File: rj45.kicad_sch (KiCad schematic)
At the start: 6 parts, among them J6 RJ45_HC612601A-M893-A

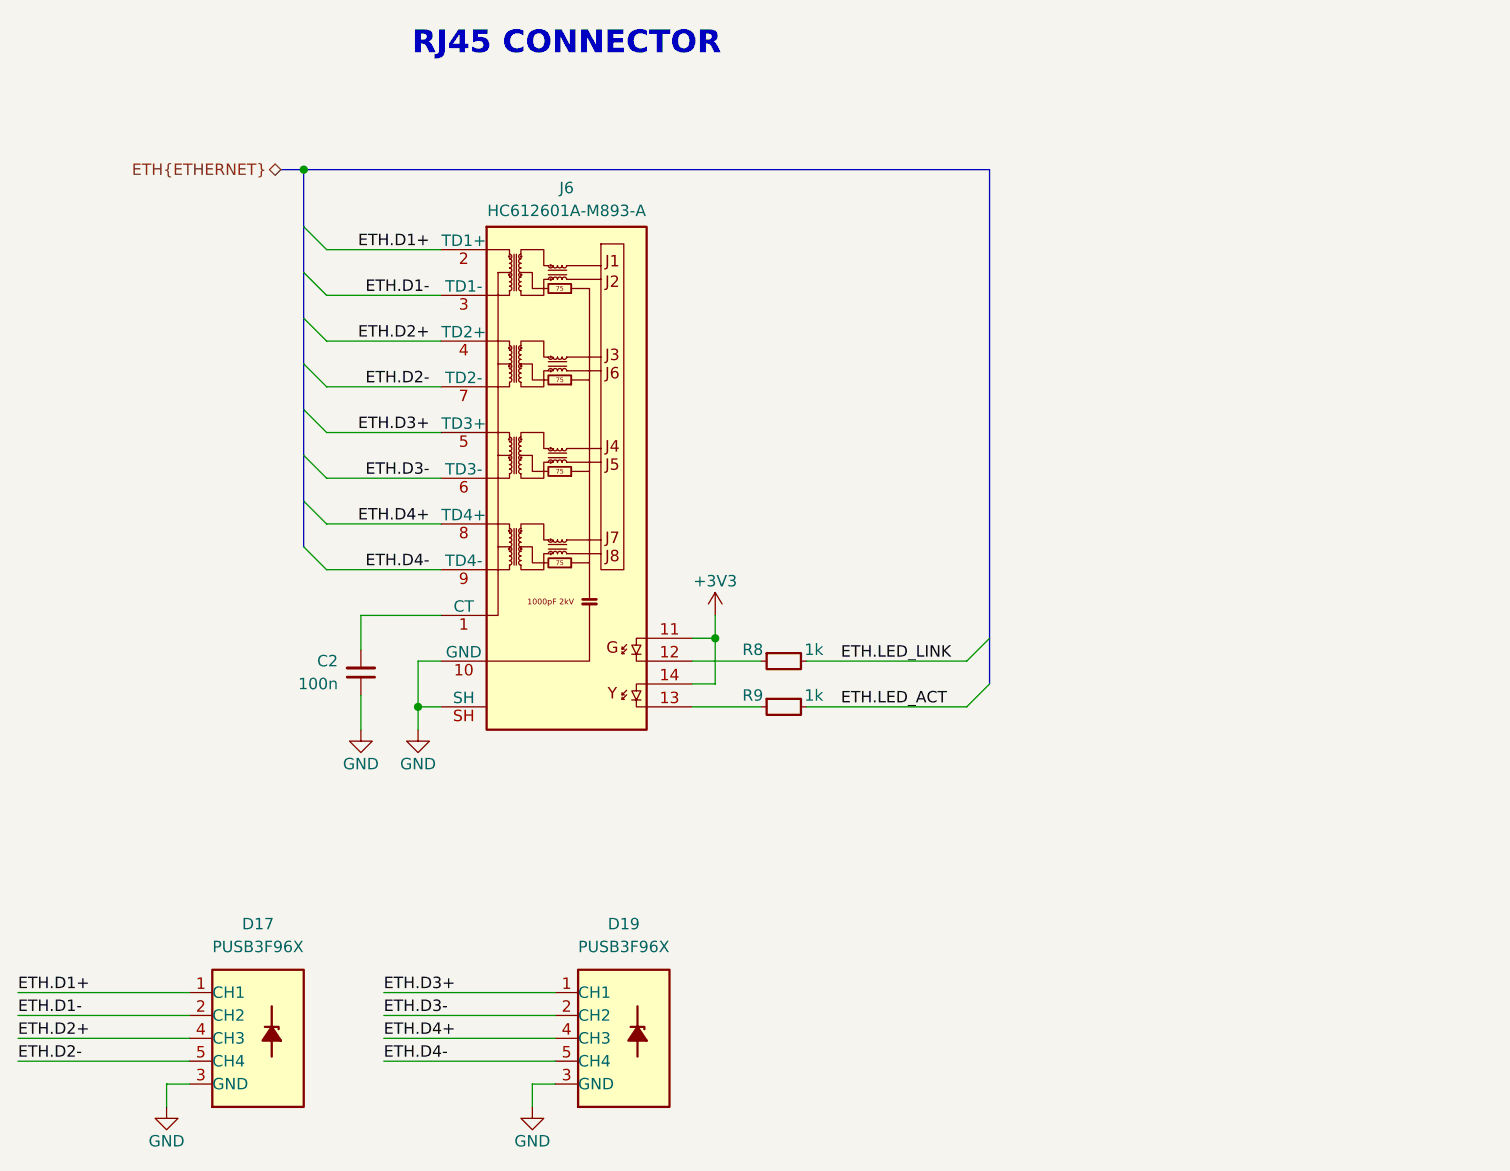
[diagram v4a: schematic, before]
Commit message: [#3] WIP: Clear ERC, re-annotate schematic
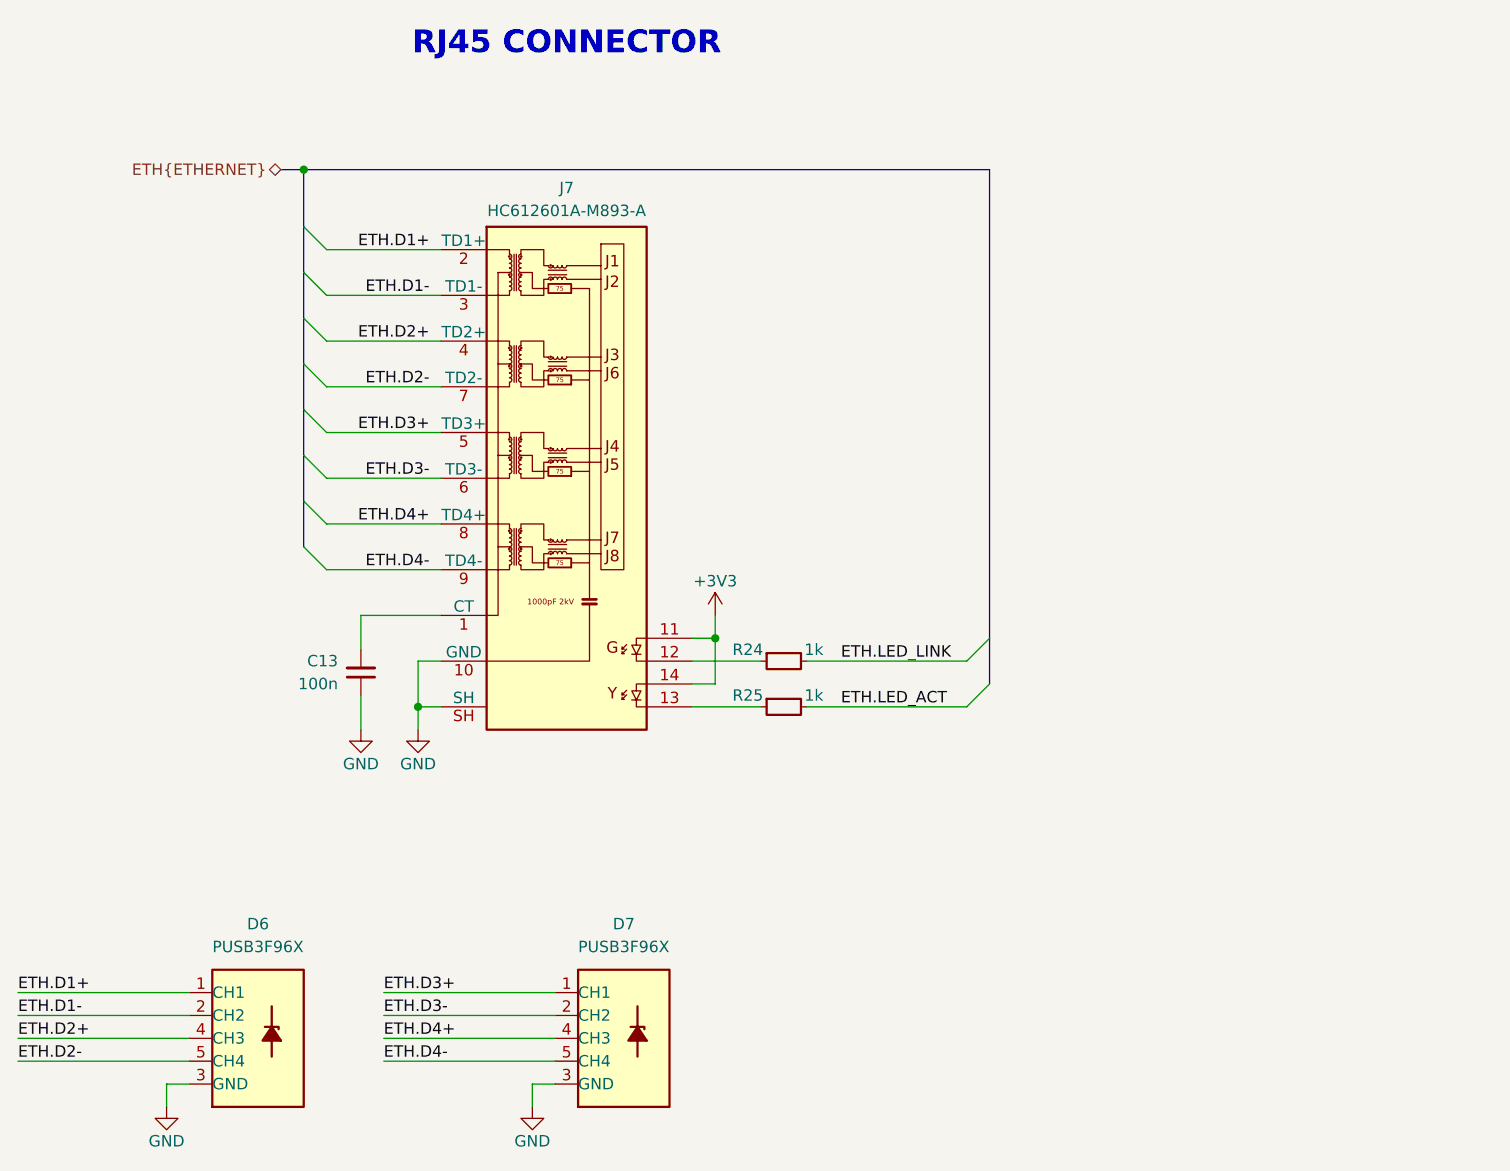
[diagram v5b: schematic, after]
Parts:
- renumbered C2 to C13, D17 to D6, D19 to D7, J6 to J7, R8 to R24, R9 to R25
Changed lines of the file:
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@@
 		(on_board yes)
 		(dnp no)
-		(property "Reference" "#PWR0193"
+		(property "Reference" "#PWR057"
 			(at 102.87 184.15 0)
 			(effects
@@
 			(project "cm5-module"
 				(path "/090a8e41-87a8-4fb1-998b-60a2c0dc4cee/dd50f821-f925-406c-ae05-a2a500dfc6d6"
-					(reference "#PWR0193")
+					(reference "#PWR057")
 					(unit 1)
 				)
@@
 		(on_board yes)
 		(dnp no)
-		(property "Reference" "#PWR031"
+		(property "Reference" "#PWR056"
 			(at 130.81 142.24 0)
 			(effects
@@
 			(project "cm5-module"
 				(path "/090a8e41-87a8-4fb1-998b-60a2c0dc4cee/dd50f821-f925-406c-ae05-a2a500dfc6d6"
-					(reference "#PWR031")
+					(reference "#PWR056")
 					(unit 1)
 				)
@@
 		(on_board yes)
 		(dnp no)
-		(property "Reference" "#PWR029"
+		(property "Reference" "#PWR054"
 			(at 163.83 127 0)
 			(effects
@@
 			(project ""
 				(path "/090a8e41-87a8-4fb1-998b-60a2c0dc4cee/dd50f821-f925-406c-ae05-a2a500dfc6d6"
-					(reference "#PWR029")
+					(reference "#PWR054")
 					(unit 1)
 				)
@@
 		(dnp no)
 		(fields_autoplaced yes)
-		(property "Reference" "D17"
+		(property "Reference" "D6"
 			(at 113.03 157.48 0)
 			(effects
@@
 			(project "cm5-module"
 				(path "/090a8e41-87a8-4fb1-998b-60a2c0dc4cee/dd50f821-f925-406c-ae05-a2a500dfc6d6"
-					(reference "D17")
+					(reference "D6")
 					(unit 1)
 				)
@@
 		(on_board yes)
 		(dnp no)
-		(property "Reference" "R9"
+		(property "Reference" "R25"
 			(at 169.164 132.08 0)
 			(effects
@@
 			(project "cm5-module"
 				(path "/090a8e41-87a8-4fb1-998b-60a2c0dc4cee/dd50f821-f925-406c-ae05-a2a500dfc6d6"
-					(reference "R9")
+					(reference "R25")
 					(unit 1)
 				)
@@
 		(on_board yes)
 		(dnp no)
-		(property "Reference" "R8"
+		(property "Reference" "R24"
 			(at 169.164 127 0)
 			(effects
@@
 			(project ""
 				(path "/090a8e41-87a8-4fb1-998b-60a2c0dc4cee/dd50f821-f925-406c-ae05-a2a500dfc6d6"
-					(reference "R8")
+					(reference "R24")
 					(unit 1)
 				)
@@
 		(on_board yes)
 		(dnp no)
-		(property "Reference" "#PWR0194"
+		(property "Reference" "#PWR058"
 			(at 143.51 184.15 0)
 			(effects
@@
 			(project "cm5-module"
 				(path "/090a8e41-87a8-4fb1-998b-60a2c0dc4cee/dd50f821-f925-406c-ae05-a2a500dfc6d6"
-					(reference "#PWR0194")
+					(reference "#PWR058")
 					(unit 1)
 				)
@@
 		(on_board yes)
 		(dnp no)
-		(property "Reference" "J6"
+		(property "Reference" "J7"
 			(at 147.32 75.692 0)
 			(effects
@@
 			(project ""
 				(path "/090a8e41-87a8-4fb1-998b-60a2c0dc4cee/dd50f821-f925-406c-ae05-a2a500dfc6d6"
-					(reference "J6")
+					(reference "J7")
 					(unit 1)
 				)
@@
 		(on_board yes)
 		(dnp no)
-		(property "Reference" "#PWR030"
+		(property "Reference" "#PWR055"
 			(at 124.46 142.24 0)
 			(effects
@@
 			(project "cm5-module"
 				(path "/090a8e41-87a8-4fb1-998b-60a2c0dc4cee/dd50f821-f925-406c-ae05-a2a500dfc6d6"
-					(reference "#PWR030")
+					(reference "#PWR055")
 					(unit 1)
 				)
@@
 		(on_board yes)
 		(dnp no)
-		(property "Reference" "C2"
+		(property "Reference" "C13"
 			(at 121.92 128.2636 90)
 			(effects
@@
 			(project "cm5-module"
 				(path "/090a8e41-87a8-4fb1-998b-60a2c0dc4cee/dd50f821-f925-406c-ae05-a2a500dfc6d6"
-					(reference "C2")
+					(reference "C13")
 					(unit 1)
 				)
@@
 		(dnp no)
 		(fields_autoplaced yes)
-		(property "Reference" "D19"
+		(property "Reference" "D7"
 			(at 153.67 157.48 0)
 			(effects
@@
 			(project "cm5-module"
 				(path "/090a8e41-87a8-4fb1-998b-60a2c0dc4cee/dd50f821-f925-406c-ae05-a2a500dfc6d6"
-					(reference "D19")
+					(reference "D7")
 					(unit 1)
 				)

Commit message: [#3] Re-annotate schematic
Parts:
- renumbered C13 to C76, D6 to D22, D7 to D23, J7 to J13, R24 to R83, R25 to R84
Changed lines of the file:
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@@
 		(on_board yes)
 		(dnp no)
-		(property "Reference" "#PWR057"
+		(property "Reference" "#PWR0194"
 			(at 102.87 184.15 0)
 			(effects
@@
 			(project "cm5-module"
 				(path "/090a8e41-87a8-4fb1-998b-60a2c0dc4cee/dd50f821-f925-406c-ae05-a2a500dfc6d6"
-					(reference "#PWR057")
+					(reference "#PWR0194")
 					(unit 1)
 				)
@@
 		(on_board yes)
 		(dnp no)
-		(property "Reference" "#PWR056"
+		(property "Reference" "#PWR0193"
 			(at 130.81 142.24 0)
 			(effects
@@
 			(project "cm5-module"
 				(path "/090a8e41-87a8-4fb1-998b-60a2c0dc4cee/dd50f821-f925-406c-ae05-a2a500dfc6d6"
-					(reference "#PWR056")
+					(reference "#PWR0193")
 					(unit 1)
 				)
@@
 		(on_board yes)
 		(dnp no)
-		(property "Reference" "#PWR054"
+		(property "Reference" "#PWR0191"
 			(at 163.83 127 0)
 			(effects
@@
 			(project ""
 				(path "/090a8e41-87a8-4fb1-998b-60a2c0dc4cee/dd50f821-f925-406c-ae05-a2a500dfc6d6"
-					(reference "#PWR054")
+					(reference "#PWR0191")
 					(unit 1)
 				)
@@
 		(dnp no)
 		(fields_autoplaced yes)
-		(property "Reference" "D6"
+		(property "Reference" "D22"
 			(at 113.03 157.48 0)
 			(effects
@@
 			(project "cm5-module"
 				(path "/090a8e41-87a8-4fb1-998b-60a2c0dc4cee/dd50f821-f925-406c-ae05-a2a500dfc6d6"
-					(reference "D6")
+					(reference "D22")
 					(unit 1)
 				)
@@
 		(on_board yes)
 		(dnp no)
-		(property "Reference" "R25"
+		(property "Reference" "R84"
 			(at 169.164 132.08 0)
 			(effects
@@
 			(project "cm5-module"
 				(path "/090a8e41-87a8-4fb1-998b-60a2c0dc4cee/dd50f821-f925-406c-ae05-a2a500dfc6d6"
-					(reference "R25")
+					(reference "R84")
 					(unit 1)
 				)
@@
 		(on_board yes)
 		(dnp no)
-		(property "Reference" "R24"
+		(property "Reference" "R83"
 			(at 169.164 127 0)
 			(effects
@@
 			(project ""
 				(path "/090a8e41-87a8-4fb1-998b-60a2c0dc4cee/dd50f821-f925-406c-ae05-a2a500dfc6d6"
-					(reference "R24")
+					(reference "R83")
 					(unit 1)
 				)
@@
 		(on_board yes)
 		(dnp no)
-		(property "Reference" "#PWR058"
+		(property "Reference" "#PWR0195"
 			(at 143.51 184.15 0)
 			(effects
@@
 			(project "cm5-module"
 				(path "/090a8e41-87a8-4fb1-998b-60a2c0dc4cee/dd50f821-f925-406c-ae05-a2a500dfc6d6"
-					(reference "#PWR058")
+					(reference "#PWR0195")
 					(unit 1)
 				)
@@
 		(on_board yes)
 		(dnp no)
-		(property "Reference" "J7"
+		(property "Reference" "J13"
 			(at 147.32 75.692 0)
 			(effects
@@
 			(project ""
 				(path "/090a8e41-87a8-4fb1-998b-60a2c0dc4cee/dd50f821-f925-406c-ae05-a2a500dfc6d6"
-					(reference "J7")
+					(reference "J13")
 					(unit 1)
 				)
@@
 		(on_board yes)
 		(dnp no)
-		(property "Reference" "#PWR055"
+		(property "Reference" "#PWR0192"
 			(at 124.46 142.24 0)
 			(effects
@@
 			(project "cm5-module"
 				(path "/090a8e41-87a8-4fb1-998b-60a2c0dc4cee/dd50f821-f925-406c-ae05-a2a500dfc6d6"
-					(reference "#PWR055")
+					(reference "#PWR0192")
 					(unit 1)
 				)
@@
 		(on_board yes)
 		(dnp no)
-		(property "Reference" "C13"
+		(property "Reference" "C76"
 			(at 121.92 128.2636 90)
 			(effects
@@
 			(project "cm5-module"
 				(path "/090a8e41-87a8-4fb1-998b-60a2c0dc4cee/dd50f821-f925-406c-ae05-a2a500dfc6d6"
-					(reference "C13")
+					(reference "C76")
 					(unit 1)
 				)
@@
 		(dnp no)
 		(fields_autoplaced yes)
-		(property "Reference" "D7"
+		(property "Reference" "D23"
 			(at 153.67 157.48 0)
 			(effects
@@
 			(project "cm5-module"
 				(path "/090a8e41-87a8-4fb1-998b-60a2c0dc4cee/dd50f821-f925-406c-ae05-a2a500dfc6d6"
-					(reference "D7")
+					(reference "D23")
 					(unit 1)
 				)

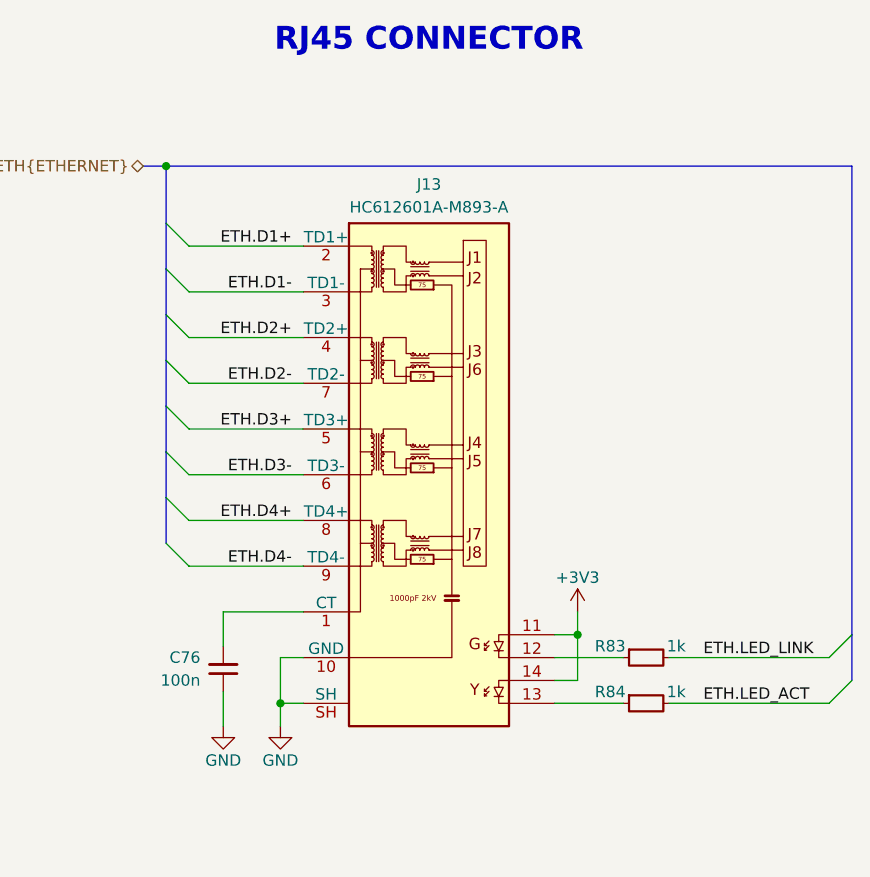
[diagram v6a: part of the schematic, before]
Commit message: [#3] Add GND pours on top and bottom
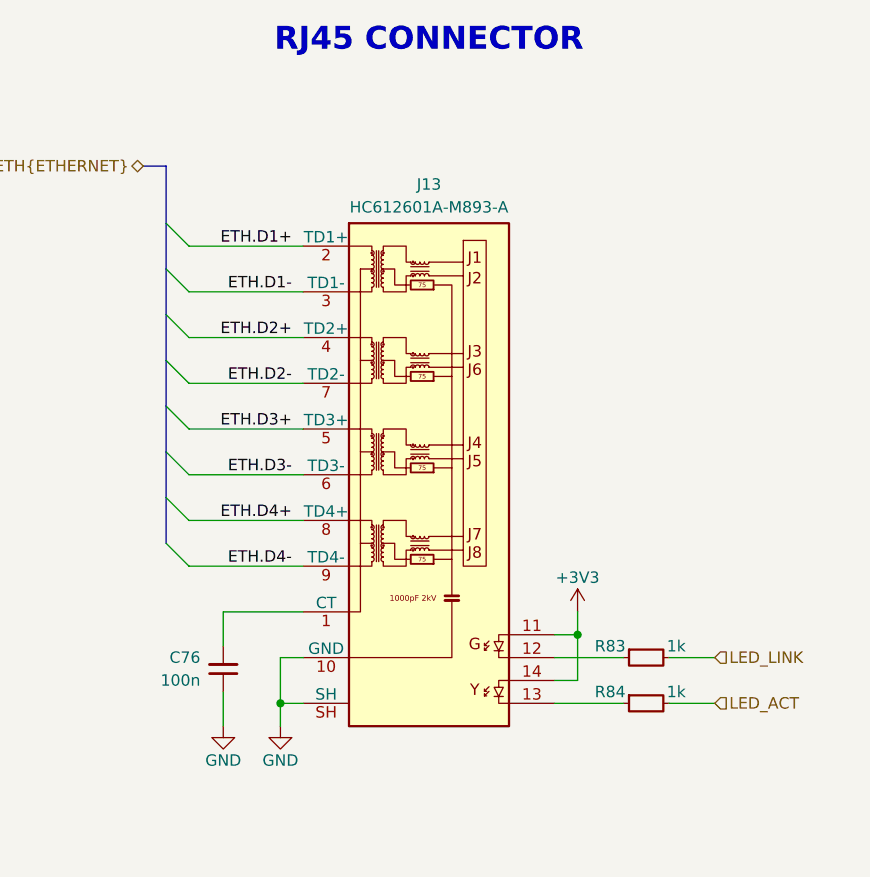
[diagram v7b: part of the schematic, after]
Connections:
- net ETH.LED_ACT renamed LED_ACT
- net ETH.LED_LINK renamed LED_LINK
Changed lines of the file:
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@@
-	)
-	(junction
-		(at 118.11 73.66)
-		(diameter 0)
-		(color 0 0 0 0)
 	)
 	(junction
@@
 	)
 	(bus_entry
-		(at 194.31 130.81)
-		(size -2.54 2.54)
-		(stroke
-			(width 0)
-			(type default)
-		)
-	)
-	(bus_entry
 		(at 120.65 107.95)
 		(size -2.54 -2.54)
@@
 		)
 	)
-	(bus_entry
-		(at 194.31 125.73)
-		(size -2.54 2.54)
-		(stroke
-			(width 0)
-			(type default)
-		)
-	)
 	(wire
 		(pts
@@
 		)
 	)
-	(bus
-		(pts
-			(xy 194.31 73.66) (xy 194.31 125.73)
-		)
-		(stroke
-			(width 0)
-			(type default)
-		)
-	)
 	(wire
 		(pts
@@
 	(wire
 		(pts
-			(xy 173.99 128.27) (xy 191.77 128.27)
+			(xy 173.99 128.27) (xy 179.07 128.27)
 		)
 		(stroke
@@
 	(wire
 		(pts
-			(xy 173.99 133.35) (xy 191.77 133.35)
+			(xy 173.99 133.35) (xy 179.07 133.35)
 		)
 		(stroke
@@
 		)
 	)
-	(bus
-		(pts
-			(xy 118.11 73.66) (xy 194.31 73.66)
-		)
-		(stroke
-			(width 0)
-			(type default)
-		)
-	)
 	(wire
 		(pts
@@
 		(pts
 			(xy 146.05 175.26) (xy 143.51 175.26)
-		)
-		(stroke
-			(width 0)
-			(type default)
-		)
-	)
-	(bus
-		(pts
-			(xy 194.31 130.81) (xy 194.31 125.73)
 		)
 		(stroke
@@
 		)
 	)
-	(label "ETH.LED_LINK"
-		(at 177.8 128.27 0)
-		(effects
-			(font
-				(size 1.27 1.27)
-			)
-			(justify left bottom)
-		)
-	)
 	(label "ETH.D4-"
 		(at 132.08 118.11 180)
@@
 		)
 	)
-	(label "ETH.LED_ACT"
-		(at 177.8 133.35 0)
-		(effects
-			(font
-				(size 1.27 1.27)
-			)
-			(justify left bottom)
-		)
-	)
 	(label "ETH.D4+"
 		(at 127 170.18 0)
@@
 		)
 	)
+	(hierarchical_label "LED_ACT"
+		(shape input)
+		(at 179.07 133.35 0)
+		(effects
+			(font
+				(size 1.27 1.27)
+			)
+			(justify left)
+		)
+	)
+	(hierarchical_label "LED_LINK"
+		(shape input)
+		(at 179.07 128.27 0)
+		(effects
+			(font
+				(size 1.27 1.27)
+			)
+			(justify left)
+		)
+	)
